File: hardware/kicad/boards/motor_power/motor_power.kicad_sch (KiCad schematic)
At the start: 58 parts, among them J1 PWM fra MCU, J2 MCP PWM, J3 DC Motor, J4 3-fase ind, J5 3-fase ud, J6 V1 ud til load, J7 Screw_Terminal_01x03, Q1 IRF540N, Q2 IRF530, SW1 Switch, U1 MCP601, U2 NE555, U3 ILD74, U4 MCP601, U5 IR2110, U6 LM7805, U7 4N25, U8 IR2110

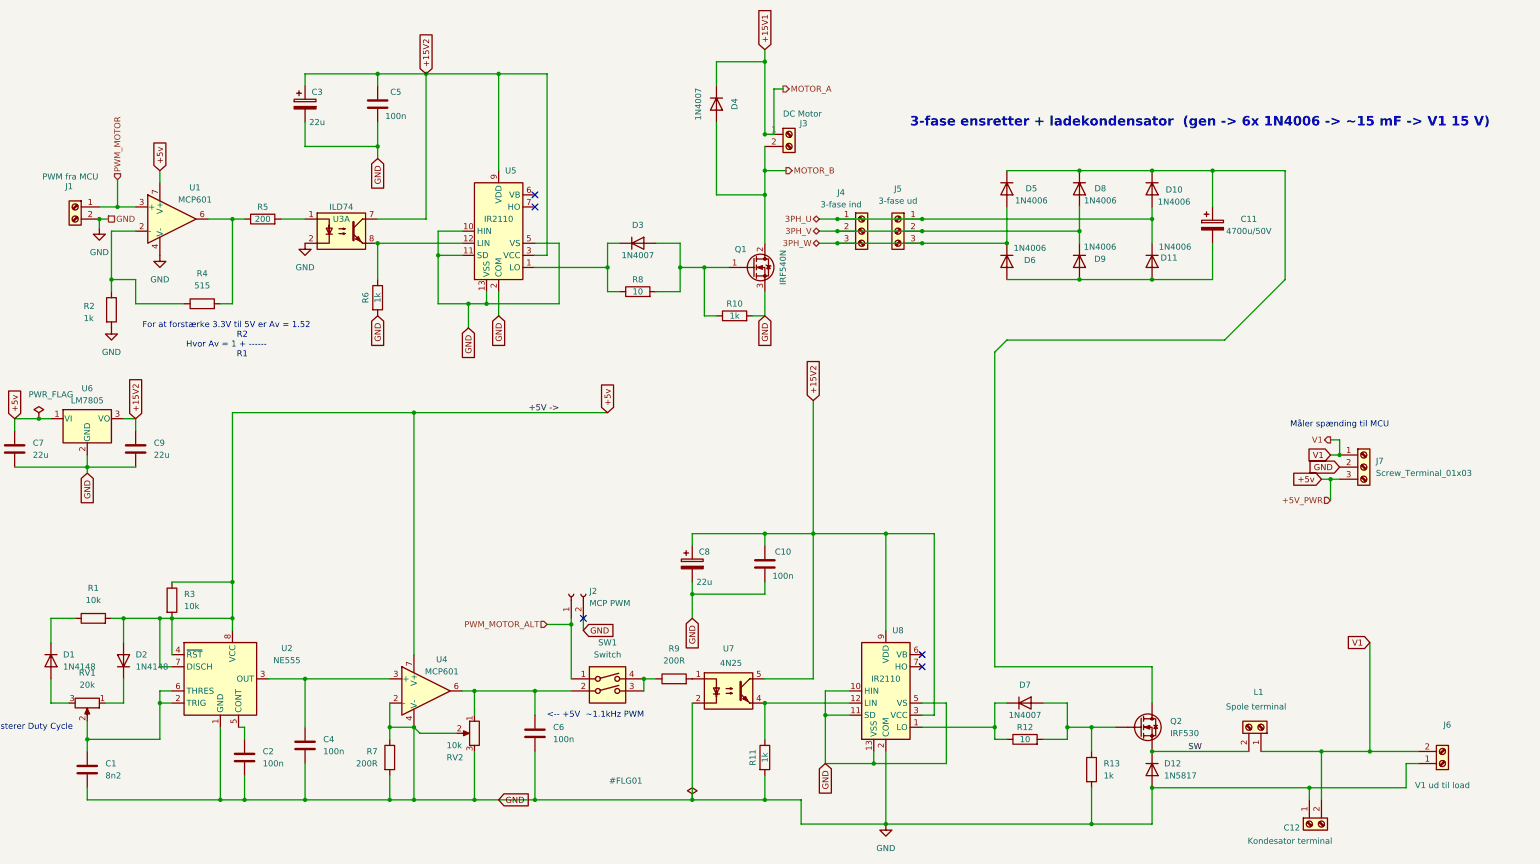
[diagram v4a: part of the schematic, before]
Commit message: system: connected top sheet for the integrated PCB
Rebuild system.kicad_sch as the netlist-connected 5-board hierarchy
(motor_power, motor_feedback, mppt_buck, boost_v2_mill, c2000_feedback),
replacing the old block-diagram. Connectivity by global labels.

- J_ARD (Arduino), J_C2K (C2000), J_INA (PV INA219) connectors
- external screw terminals: 3-phase, motor, PV, store, load, +15V, +5V
- 17 diagnostic probe-point headers on the key nets
- single GND<->GND_MCU star tie (R_STAR 0R)
- generator tools/generators/build_system_top.py (reference; the sheet is
  now hand-maintained in the GUI)

Netlist verified: all 36 top-level connector pins match the interface
contract, no shorts, STORE/V1/LOAD buses span the right boards. Sub-sheet
.kicad_sch carry hierarchical instance data from opening the hierarchy.
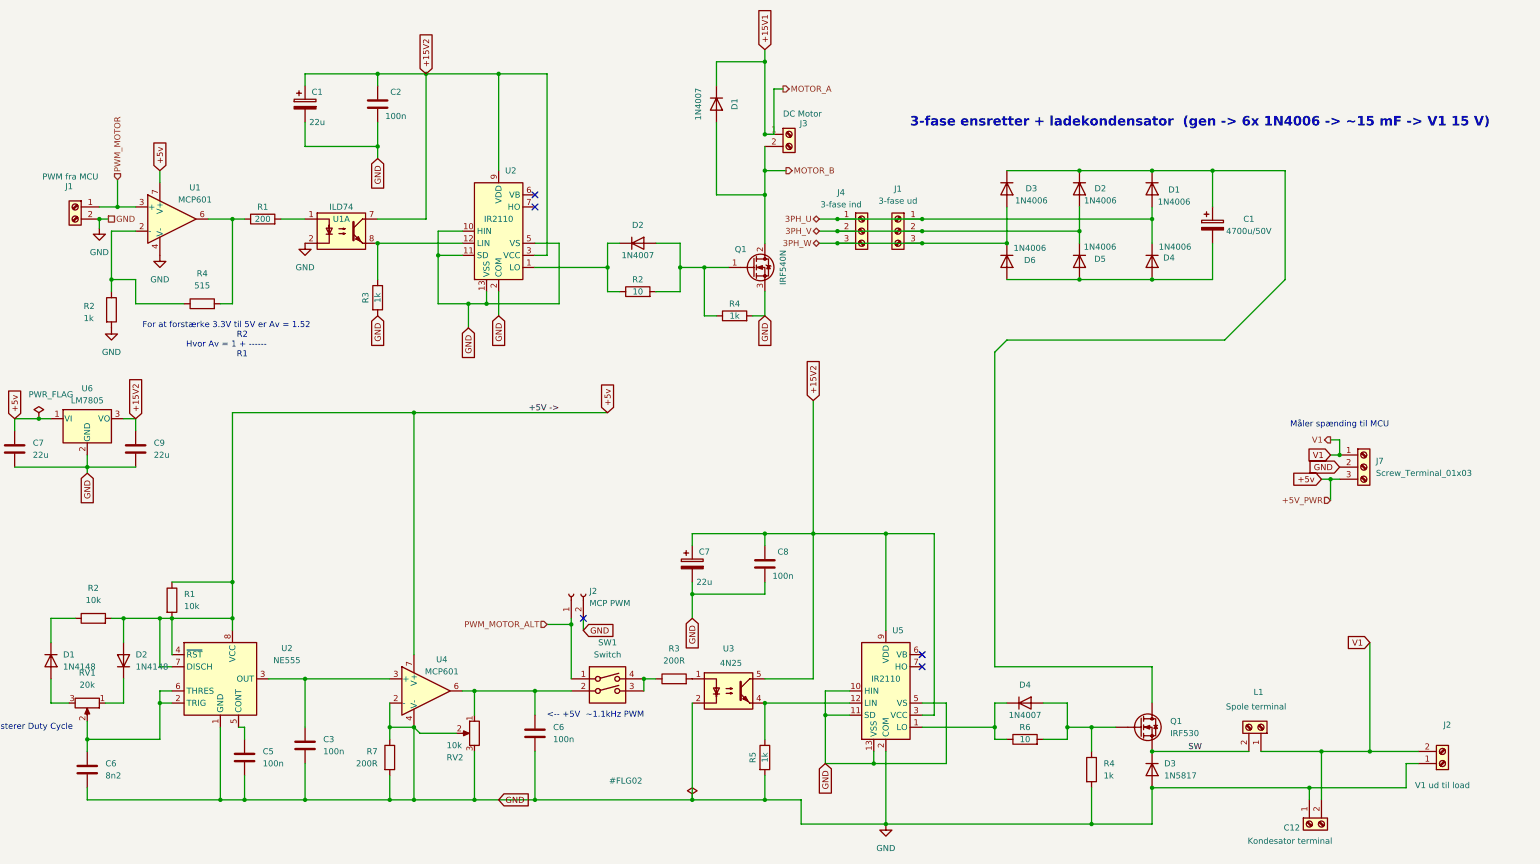
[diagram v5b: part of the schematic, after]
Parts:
- renumbered C3 to C1, C11 to C1, C5 to C2, C4 to C3, C2 to C5, C1 to C6, C8 to C7, C10 to C8, D10 to D1, D4 to D1, D3 to D2, D8 to D2, D12 to D3, D5 to D3, D11 to D4, D7 to D4, D9 to D5, J5 to J1, J6 to J2, Q2 to Q1, R3 to R1, R5 to R1, R8 to R2, R1 to R2, R6 to R3, R9 to R3, R13 to R4, R10 to R4, R11 to R5, R12 to R6, U3 to U1, U5 to U2, U7 to U3, U8 to U5

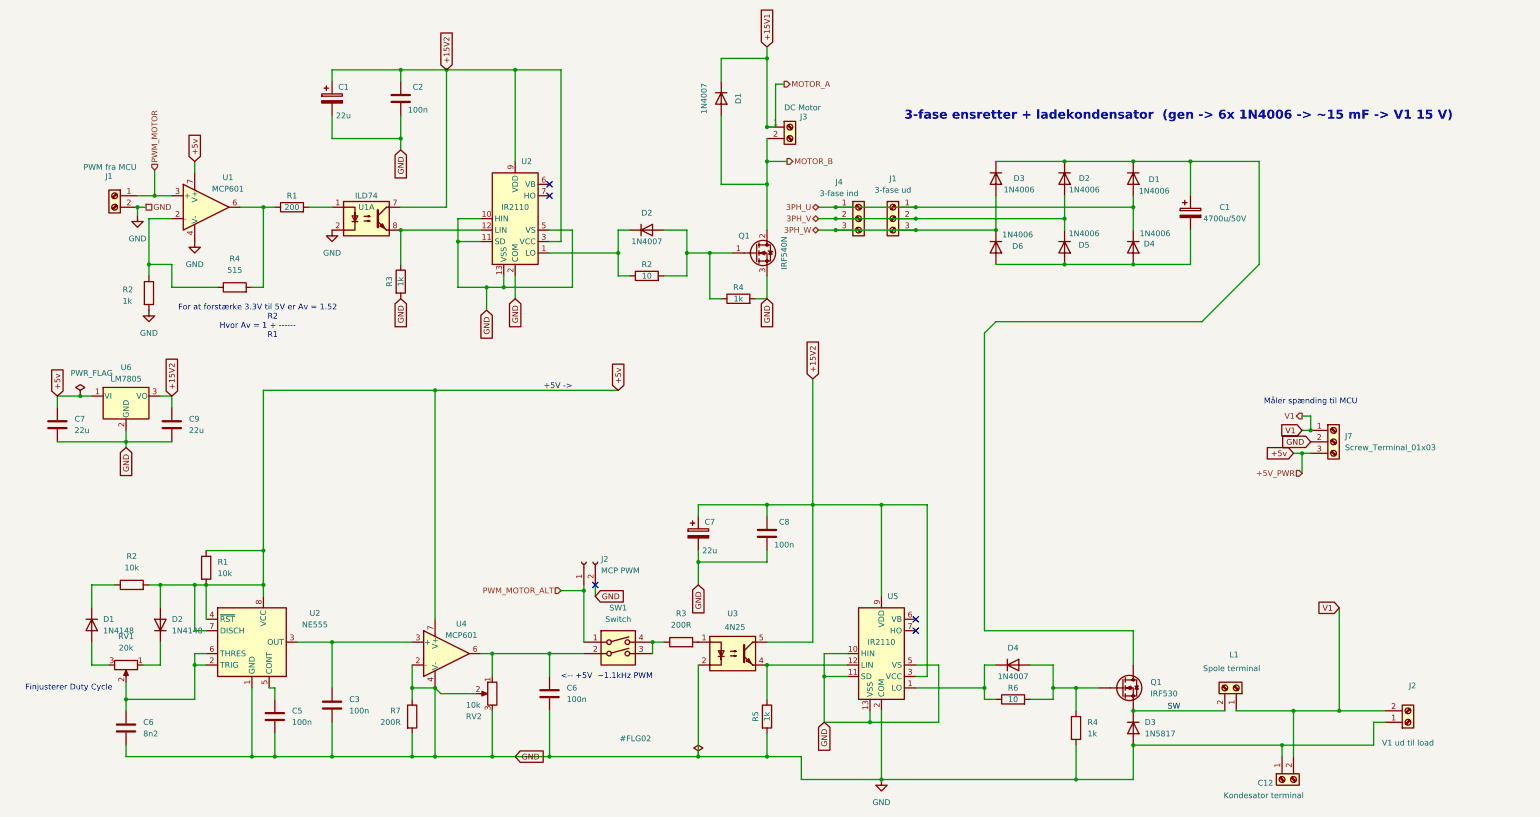
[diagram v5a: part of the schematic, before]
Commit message: system: single edge-connector set + integrated board
- delete 22 redundant board-level I/O connectors (J201-207, J301-302,
  J401-404, J501-504, J601-605); on the monolithic board these are internal
  board-to-board nets (now copper traces) or duplicates of the top-level edge
  set. Nets carried by the hierarchical sheet pins; netlist re-verified.
- C212: real capacitor footprint, + on V1 (was a swap terminal)
- motor_feedback MCU-side powered from +5V_PWR (merged +5V_MCU)
- footprints assigned to all top-level connectors/probes (J_*, TP, R_STAR)
- system.kicad_pcb: integrated board pulled via Update-PCB-from-Schematic
- placement guide (PNG + PDF) + generator/patch scripts
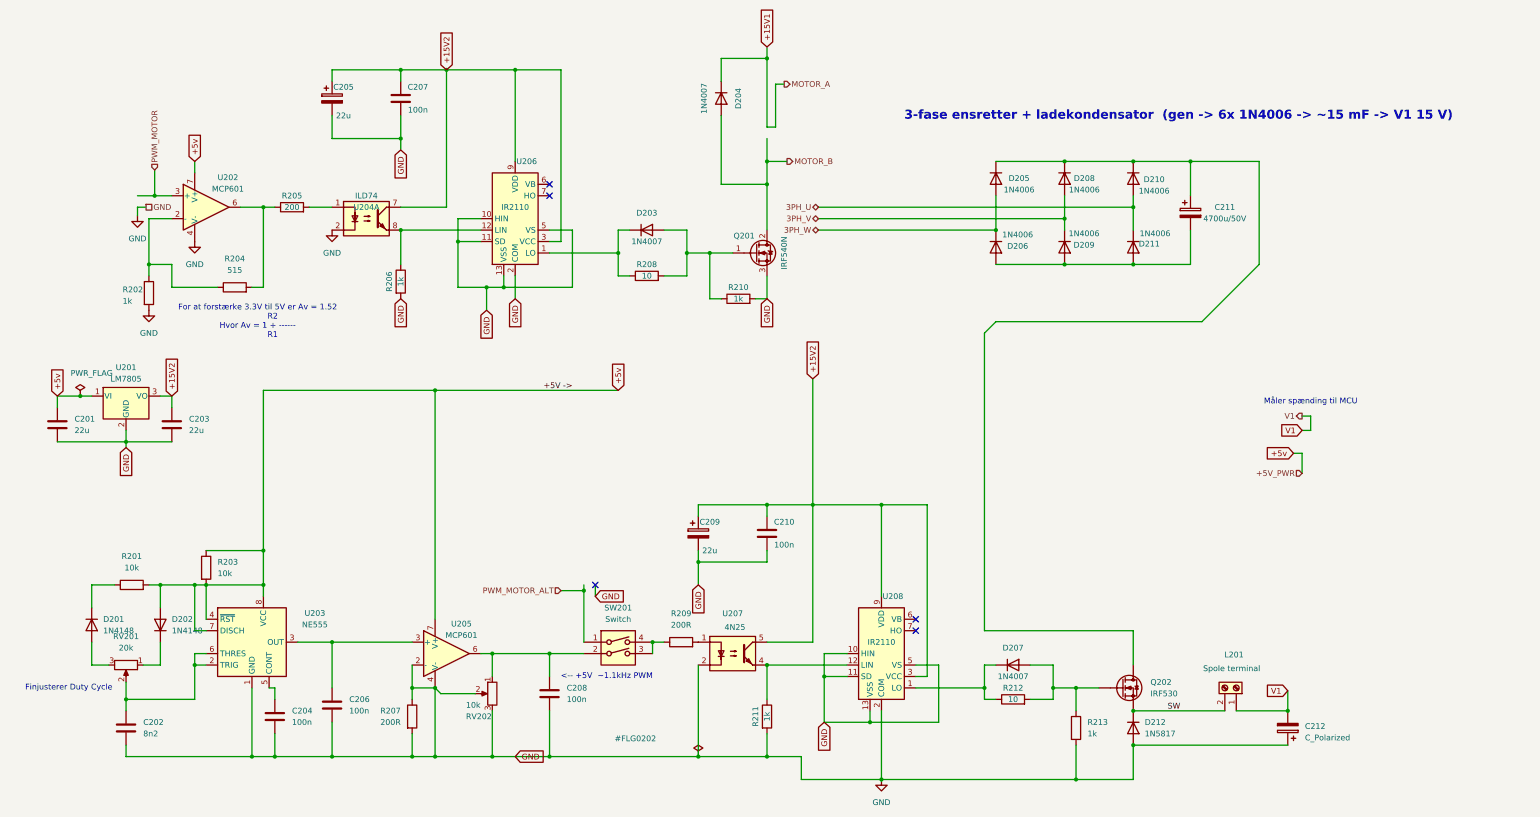
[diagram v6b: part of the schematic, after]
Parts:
- removed C12: Kondesator terminal, TerminalBlock:TerminalBlock_bornier-2_P5.08mm, symbol Connector:Screw_Terminal_01x02
- removed J1: 3-fase ud, TerminalBlock:TerminalBlock_bornier-3_P5.08mm, symbol Connector:Screw_Terminal_01x03
- removed J1: PWM fra MCU, TerminalBlock:TerminalBlock_bornier-2_P5.08mm, symbol Connector:Screw_Terminal_01x02
- removed J2: MCP PWM, Connector_PinHeader_2.54mm:PinHeader_1x02_P2.54mm_Vertical, symbol Connector:Conn_01x02_Socket
- removed J2: V1 ud til load, TerminalBlock:TerminalBlock_bornier-2_P5.08mm, symbol Connector:Screw_Terminal_01x02
- removed J3: DC Motor, TerminalBlock:TerminalBlock_bornier-2_P5.08mm, symbol Connector:Screw_Terminal_01x02
- removed J4: 3-fase ind, TerminalBlock:TerminalBlock_bornier-3_P5.08mm, symbol Connector:Screw_Terminal_01x03
- removed J7: Screw_Terminal_01x03, TerminalBlock:TerminalBlock_bornier-3_P5.08mm, symbol Connector:Screw_Terminal_01x03
- added C212: C_Polarized, Capacitor_THT:CP_Radial_D8.0mm_P3.50mm, symbol Device:C_Polarized
- renumbered C7 to C201, C6 to C202, C9 to C203, C5 to C204, C1 to C205, C3 to C206, C2 to C207, C6 to C208, C7 to C209, C8 to C210, C1 to C211, D1 to D201, D2 to D202, D2 to D203, D1 to D204, D3 to D205, D6 to D206, D4 to D207, D2 to D208, D5 to D209, D1 to D210, D4 to D211, D3 to D212, L1 to L201, Q1 to Q201, Q1 to Q202, R2 to R201, R2 to R202, R1 to R203, R4 to R204, R1 to R205, R3 to R206, R7 to R207, R2 to R208, R3 to R209, R4 to R210, R5 to R211, R6 to R212, R4 to R213, RV1 to RV201, RV2 to RV202, SW1 to SW201, U6 to U201, U1 to U202, U2 to U203, U1 to U204, U4 to U205, U2 to U206, U3 to U207, U5 to U208
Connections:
- net GND: now also C212.1
- net V1: now also C212.2
